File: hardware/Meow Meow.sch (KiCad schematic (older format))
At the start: 28 parts

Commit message: Remove button reset
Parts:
- removed P?: A, symbol CONN_01X01_FEMALE
- removed P?: CLICK_LEFT, symbol CONN_01X01_FEMALE
- removed P?: W, symbol CONN_01X01_FEMALE
- removed P?: LEFT, symbol CONN_01X01_FEMALE
- removed P?: UP, symbol CONN_01X01_FEMALE
- removed SW?: RESET, symbol SW_Push
- added P1: CONN_01X05, Pin_Headers:Pin_Header_Straight_1x05_Pitch2.54mm, symbol CONN_01X05
- C1, C2, C3, C4, C5, C6: renamed from C?; footprint (none) -> Capacitors_SMD:C_0805_HandSoldering
- D1, D2: renamed from D?; footprint (none) -> LEDs:LED_0805_HandSoldering
- P10, P11, P12, P13, P7, P9: renamed from P?; footprint (none) -> Wire_Pads:SolderWirePad_2x_2mmDrill
- P3: renamed from P?; footprint (none) -> Connect:USB_Micro-B_10103594-0001LF
- P8: renamed from P?; value CONN_02X03 -> SWD; footprint (none) -> Pin_Headers:Pin_Header_Straight_2x03_Pitch1.00mm_SMD
- R1, R2, R3: renamed from R?; footprint (none) -> Resistors_SMD:R_0805_HandSoldering
- U1: renamed from U?; footprint SOIC127P600X160-14N -> Housings_SOIC:SO-20_12.8x7.5mm_Pitch1.27mm; Part# (none) -> ATSAMD11D14A-SSNT
- U2: renamed from U?; footprint (none) -> TO_SOT_Packages_SMD:SOT-223-3_TabPin2; Part# (none) -> AP2114HA-3.3TRG1
- Y1: renamed from Y?; Part# (none) -> LFXTAL016178Reel
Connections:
- wire segments 78 -> 75

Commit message: Version SAMD21
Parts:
- removed C3: 22pF, Capacitors_SMD:C_0805_HandSoldering, symbol C_Small
- removed P1: CONN_01X05, Pin_Headers:Pin_Header_Straight_1x05_Pitch2.54mm, symbol CONN_01X05
- removed P3: USB_micro, Connect:USB_Micro-B_10103594-0001LF, symbol USB_OTG
- removed P7: DOWN, Wire_Pads:SolderWirePad_2x_2mmDrill, symbol CONN_01X01_FEMALE
- removed U1: ATSAMD11D14A-SSNT, Housings_SOIC:SO-20_12.8x7.5mm_Pitch1.27mm, symbol ATSAMD11D14A-SSNT
- removed Y1: 32k, symbol Crystal_Small
- added F1: 0.5A, symbol Fuse_Small
- added P1: UP, MeowMeow:ALLIGATORCLIP, symbol CONN_01X01_FEMALE
- added P10, P5: CLICK_LEFT, MeowMeow:ALLIGATORCLIP, symbol CONN_01X01_FEMALE
- added P11: RIGHT, MeowMeow:ALLIGATORCLIP, symbol CONN_01X01_FEMALE
- added P8: LEFT, MeowMeow:ALLIGATORCLIP, symbol CONN_01X01_FEMALE
- added P9: USB_Micro, Connect:USB_Micro-B_10103594-0001LF, symbol USB_OTG
- added U1: ATSAMD21G15A-AU, Housings_QFP:TQFP-48_7x7mm_Pitch0.5mm, symbol ATSAMD21G18A-AU
- C1: value 0.1uF -> C_Small
- C2: value 22pF -> 0.1uF
- D1: value LED -> POWER; footprint LEDs:LED_0805_HandSoldering -> LEDs:LED-3MM
- D2: footprint LEDs:LED_0805_HandSoldering -> LEDs:LED-3MM
- P12: value CLICK -> SPACE; footprint Wire_Pads:SolderWirePad_2x_2mmDrill -> MeowMeow:ALLIGATORCLIP
- P2: renamed from P9; footprint Wire_Pads:SolderWirePad_2x_2mmDrill -> MeowMeow:ALLIGATORCLIP
- P3: renamed from P10; footprint Wire_Pads:SolderWirePad_2x_2mmDrill -> MeowMeow:ALLIGATORCLIP
- P4: renamed from P8; value SWD -> CONN_02X03; footprint Pin_Headers:Pin_Header_Straight_2x03_Pitch1.00mm_SMD -> Pin_Headers:Pin_Header_Straight_2x03_Pitch2.54mm
- P6: renamed from P11; footprint Wire_Pads:SolderWirePad_2x_2mmDrill -> MeowMeow:ALLIGATORCLIP
- P7: renamed from P13; footprint Wire_Pads:SolderWirePad_2x_2mmDrill -> MeowMeow:ALLIGATORCLIP
- R1: value 330 -> 10K
- U2: footprint TO_SOT_Packages_SMD:SOT-223-3_TabPin2 -> TO_SOT_Packages_SMD:SOT-223-3Lead_TabPin2; Part# AP2114HA-3.3TRG1 -> (none)
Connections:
- net X0/Y6 is gone; now on net Y3: P3.1
- net X1/Y7 is gone; now on net Y4: P2.1
- net +3V3: now also C2.1, R1.2, U1.17 (VDDIO1), U1.36 (VDDIO2), U1.44 (VDDIN), U1.6 (VDDANA)
- net D+: now also P9.3 (D+), U1.34 (PA25)
- net D-: now also P9.2 (D-), U1.33 (PA24)
- net GND: now also C2.2, P9.5 (GND), P9.6 (shield), U1.18 (GND1), U1.35 (GND2), U1.42 (GND3), U1.5 (GNDANA); no longer C2.1
- net RESET: now also U1.40 (~RESETN~); no longer C1.1
- net SWCLK: now also P4.5 (P5), U1.45 (PA30); no longer P4.1 (P1)
- net SWDIO: now also P4.1 (P1), U1.46 (PA31); no longer D2.2 (A), P4.5 (P5)
- net VCC: now also F1.1
- net Y0: now also U1.3 (PA02)
- net Y1: now also P6.1, U1.4 (PA03); no longer P12.1
- net Y2: now also P5.1, U1.9 (PA04); no longer P6.1
- net Y3: now also U1.10 (PA05)
- net Y4: now also U1.11 (PA06)
- net Y5: now also P12.1, U1.12 (PA07)
- new net: C1.1, U1.43 (VDDCORE)
- new net: F1.2, P9.1 (VBUS)
- new net D8: D2.2 (A), U1.38 (PB23)
- new net OSC1: U1.1 (PA00)
- new net OSC2: U1.2 (PA01)
- new net Y14: P8.1, U1.7 (PB08)
- new net Y15: P1.1, U1.8 (PB09)
- new net Y8: P11.1, U1.47 (PB02)
- new net Y9: P10.1, U1.48 (PB03)
- no-connect marks 3 -> 2
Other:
- note added: "MICROCONTROLLER SAMD21"
- note removed: "MICROCONTROLLER SAMD11"
- moved on the sheet: P2, P3, P6, P7, R1

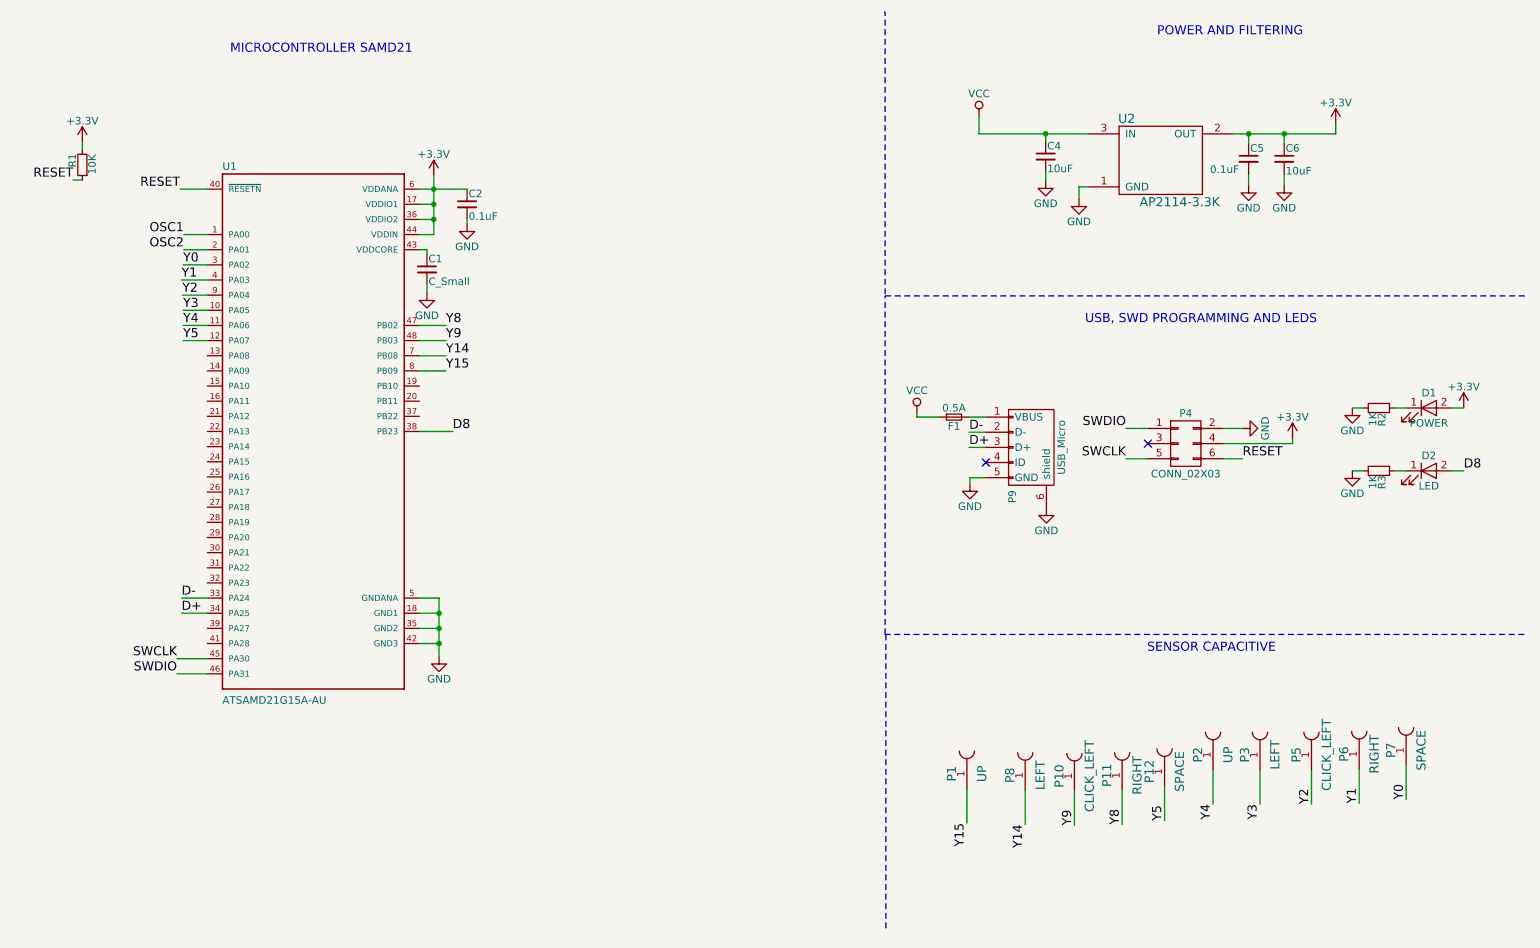
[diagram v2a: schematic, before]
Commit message: Add I2C, I2S, Serial and SPI port
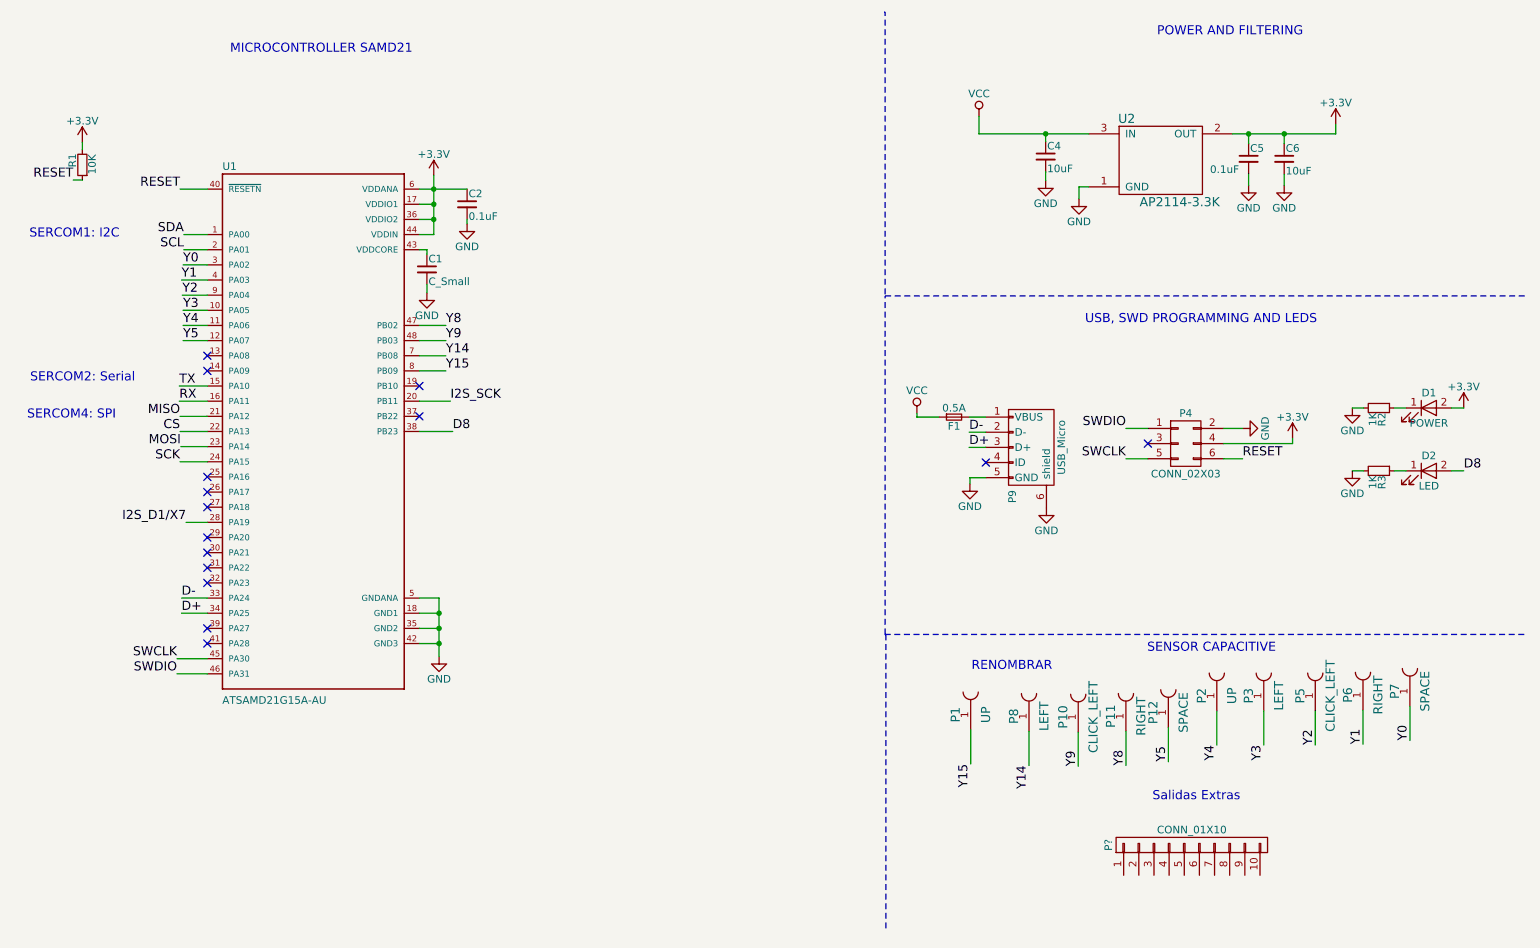
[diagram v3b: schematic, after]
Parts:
- added P?: CONN_01X10, symbol CONN_01X10
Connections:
- net TX: now reaches U1.15 (PA10)
- net RX: now reaches U1.16 (PA11)
- net I2S_SCK: now reaches U1.20 (PB11)
- net MISO: now reaches U1.21 (PA12)
- net CS: now reaches U1.22 (PA13)
- net MOSI: now reaches U1.23 (PA14)
- net SCK: now reaches U1.24 (PA15)
- net I2S_D1/X7: now reaches U1.28 (PA19)
- net OSC1 renamed SDA
- net OSC2 renamed SCL
- no-connect marks 2 -> 15
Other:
- note added: "RENOMBRAR"
- note added: "SERCOM1: I2C"
- note added: "SERCOM2: Serial"
- note added: "SERCOM4: SPI"
- note added: "Salidas Extras"
- moved on the sheet: P1, P10, P11, P12, P2, P3, P5, P6, P7, P8

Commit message: Fix label name pins X
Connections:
- net RX renamed RX/X3
- net TX renamed TX/X2
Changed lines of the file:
@@
 Text Label 2315 3255 2    60   ~ 0
 CS
-Text Label 2310 2955 0    60   ~ 0
-TX
-Text Label 2310 3055 0    60   ~ 0
-RX
+Text Label 2310 2955 2    60   ~ 0
+TX/X2
+Text Label 2310 3055 2    60   ~ 0
+RX/X3
 Wire Wire Line
 	2495 3155 2315 3155
@@
 Text Notes 1320 1985 0    60   ~ 0
 SERCOM1: I2C
-Text Notes 1325 2935 0    60   ~ 0
+Text Notes 1205 2935 0    60   ~ 0
 SERCOM2: Serial
 Wire Wire Line

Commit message: Rename pin with firmware beta and extra pins
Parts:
- removed P?: CONN_01X10, symbol CONN_01X10
- added P13: CONN_01X12, symbol CONN_01X12
- P1: value UP -> D
- P10: value CLICK_LEFT -> A
- P11: value RIGHT -> W
- P12: value SPACE -> MOUSE_LEFT
- P2: value UP -> SPACE
- P3: value LEFT -> KEY_RIGHT_ARROW
- P5: value CLICK_LEFT -> KEY_LEFT_ARROW
- P6: value RIGHT -> KEY_DOWN_ARROW
- P7: value SPACE -> KEY_UP_ARROW
- P8: value LEFT -> S
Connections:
- wire segments 83 -> 97
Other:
- note added: "PIN EXTRAS"
- note removed: "RENOMBRAR"
- note removed: "Salidas Extras"
- moved on the sheet: P1, P10, P11, P12, P8
